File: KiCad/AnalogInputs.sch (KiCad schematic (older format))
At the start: 48 parts, among them J401 AI1, J402 AI2, J403 AI3, J404 AI4, J405 AI5, J406 AI6, J407 AI7, J408 AI8, U401 ADS1115IDGST, U402 ADS1115IDGST

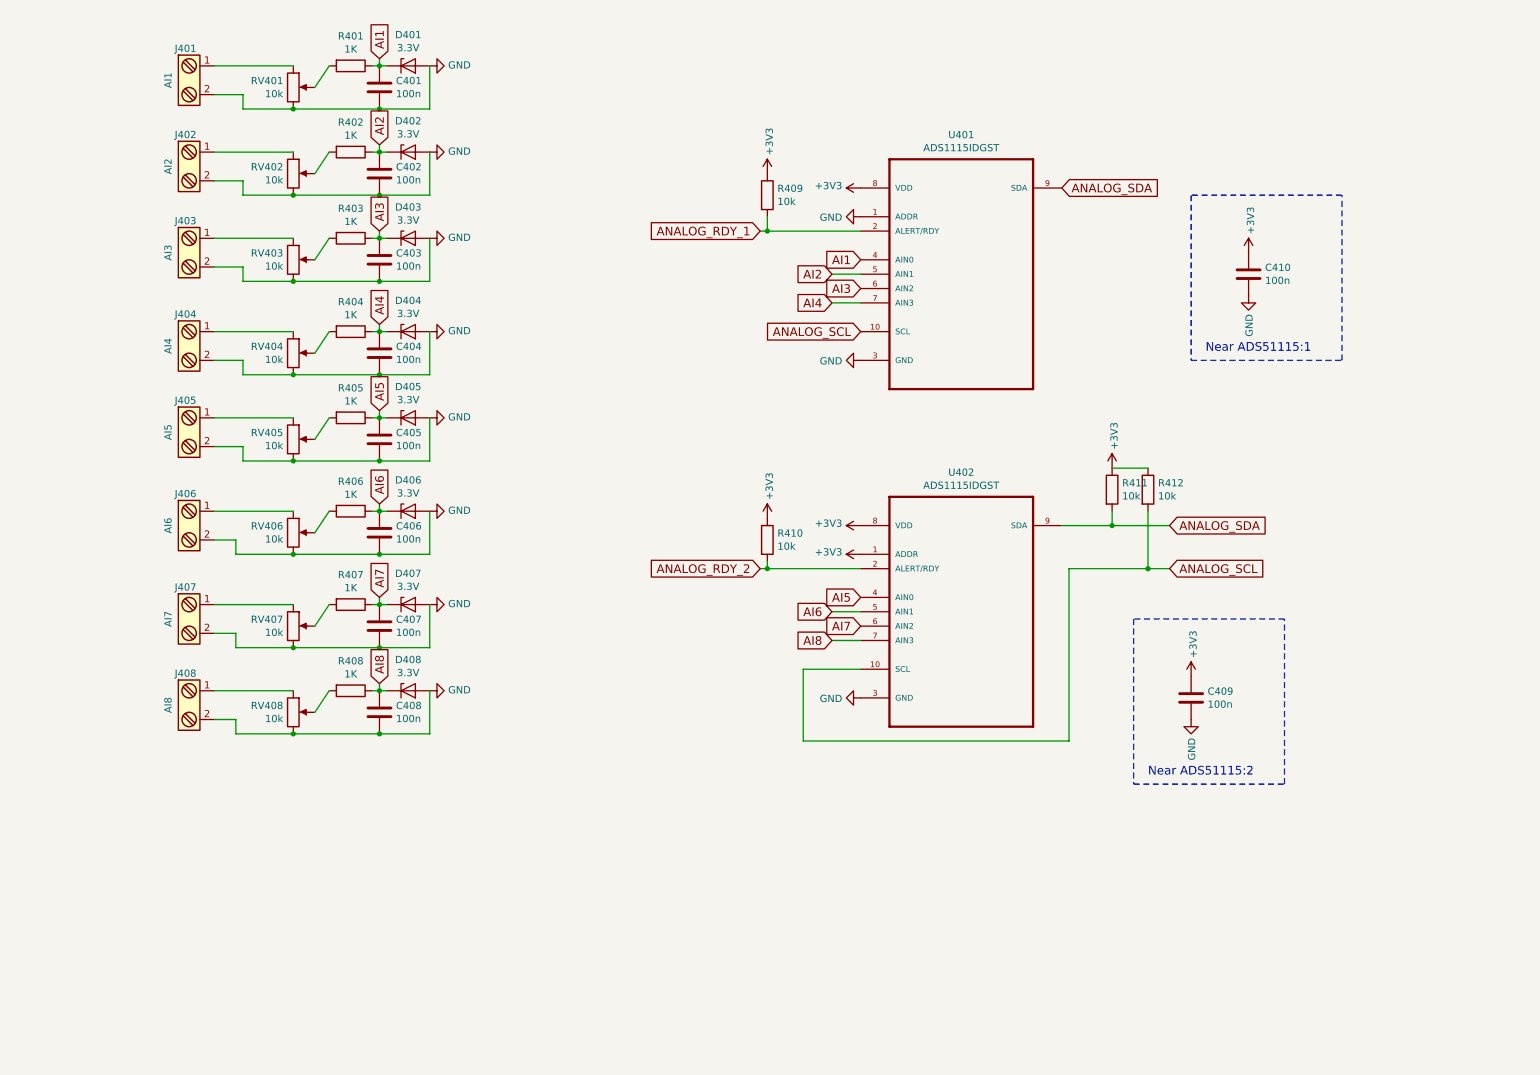
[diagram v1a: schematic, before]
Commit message: Save with sensor inputs using digital potentiometer
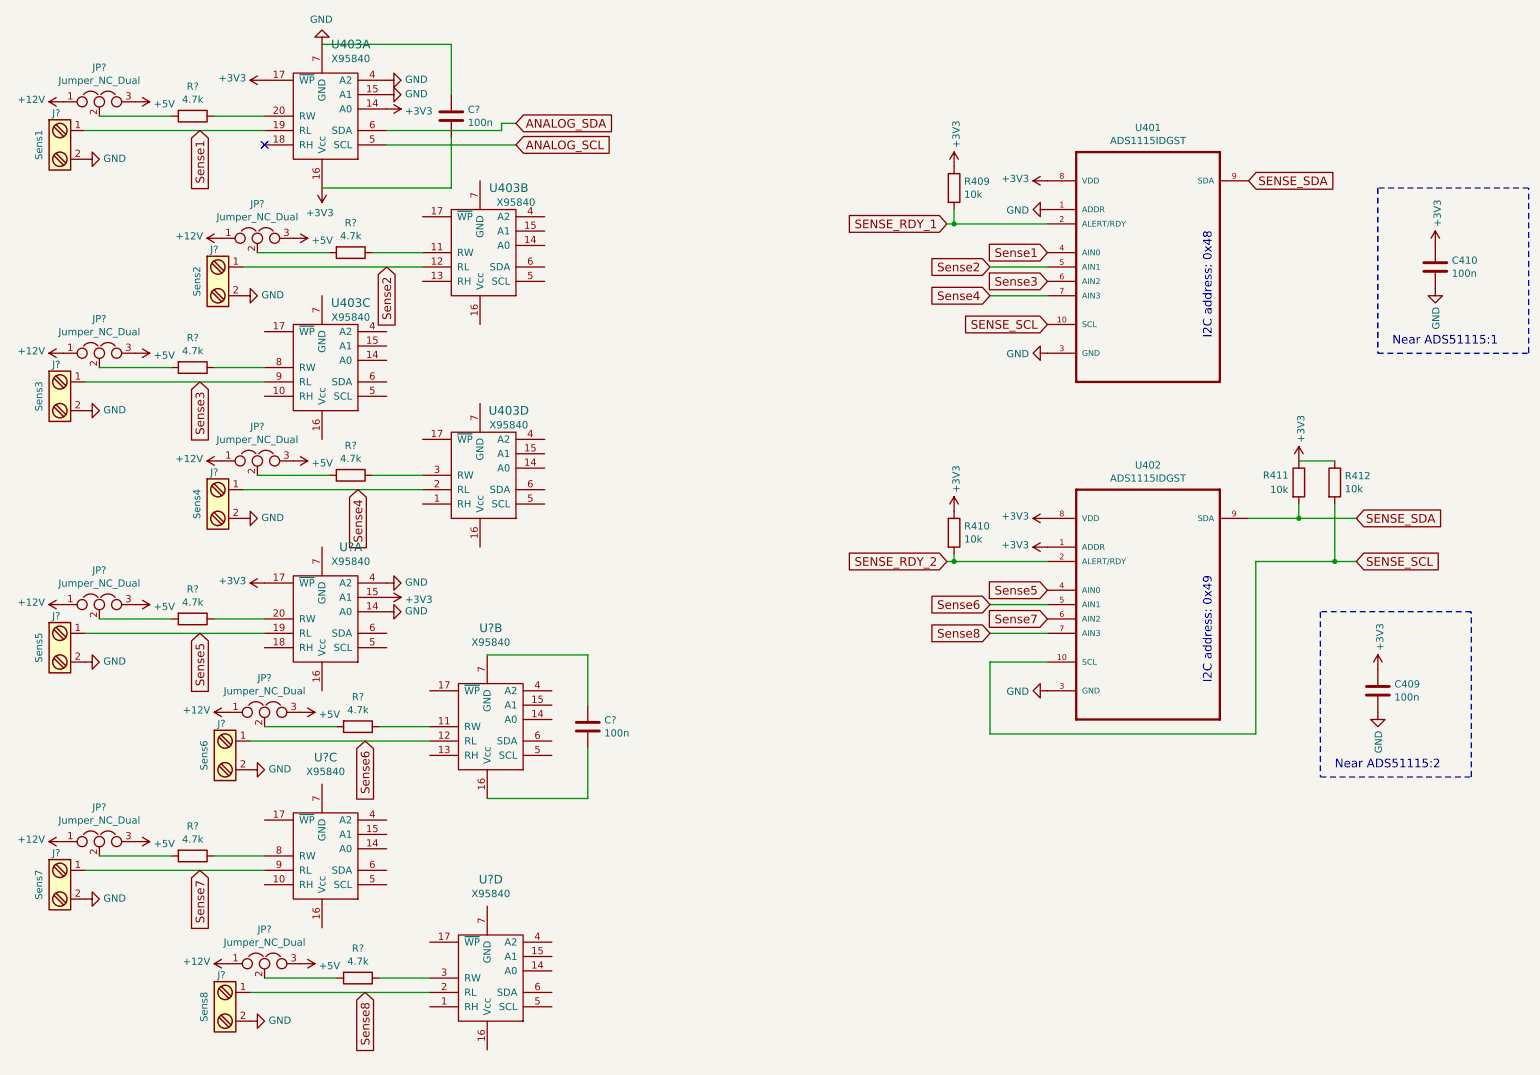
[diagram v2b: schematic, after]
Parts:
- removed C401, C402, C403, C404, C405, C406, C407, C408: 100n, Capacitors_SMD:C_0805, symbol C
- removed D401, D402, D403, D404, D405, D406, D407, D408: 3.3V, Diodes_SMD:D_SOT-23_ANK, symbol D_Zener
- removed J401: AI1, Connectors_Terminal_Blocks:TerminalBlock_Pheonix_MPT-2.54mm_2pol, symbol Screw_Terminal_1x02
- removed J402: AI2, Connectors_Terminal_Blocks:TerminalBlock_Pheonix_MPT-2.54mm_2pol, symbol Screw_Terminal_1x02
- removed J403: AI3, Connectors_Terminal_Blocks:TerminalBlock_Pheonix_MPT-2.54mm_2pol, symbol Screw_Terminal_1x02
- removed J404: AI4, Connectors_Terminal_Blocks:TerminalBlock_Pheonix_MPT-2.54mm_2pol, symbol Screw_Terminal_1x02
- removed J405: AI5, Connectors_Terminal_Blocks:TerminalBlock_Pheonix_MPT-2.54mm_2pol, symbol Screw_Terminal_1x02
- removed J406: AI6, Connectors_Terminal_Blocks:TerminalBlock_Pheonix_MPT-2.54mm_2pol, symbol Screw_Terminal_1x02
- removed J407: AI7, Connectors_Terminal_Blocks:TerminalBlock_Pheonix_MPT-2.54mm_2pol, symbol Screw_Terminal_1x02
- removed J408: AI8, Connectors_Terminal_Blocks:TerminalBlock_Pheonix_MPT-2.54mm_2pol, symbol Screw_Terminal_1x02
- removed R401, R402, R403, R404, R405, R406, R407, R408: 1K, Resistors_SMD:R_0805, symbol R
- removed RV401, RV402, RV403, RV404, RV405, RV406, RV407, RV408: 10k, Potentiometers:Potentiometer_WirePads_Small, symbol POT
- added C? (x2): 100n, Capacitors_SMD:C_0805, symbol C
- added J?: Sens1, Connectors_Terminal_Blocks:TerminalBlock_Pheonix_MPT-2.54mm_2pol, symbol Screw_Terminal_1x02
- added J?: Sens2, Connectors_Terminal_Blocks:TerminalBlock_Pheonix_MPT-2.54mm_2pol, symbol Screw_Terminal_1x02
- added J?: Sens3, Connectors_Terminal_Blocks:TerminalBlock_Pheonix_MPT-2.54mm_2pol, symbol Screw_Terminal_1x02
- added J?: Sens4, Connectors_Terminal_Blocks:TerminalBlock_Pheonix_MPT-2.54mm_2pol, symbol Screw_Terminal_1x02
- added J?: Sens5, Connectors_Terminal_Blocks:TerminalBlock_Pheonix_MPT-2.54mm_2pol, symbol Screw_Terminal_1x02
- added J?: Sens6, Connectors_Terminal_Blocks:TerminalBlock_Pheonix_MPT-2.54mm_2pol, symbol Screw_Terminal_1x02
- added J?: Sens7, Connectors_Terminal_Blocks:TerminalBlock_Pheonix_MPT-2.54mm_2pol, symbol Screw_Terminal_1x02
- added J?: Sens8, Connectors_Terminal_Blocks:TerminalBlock_Pheonix_MPT-2.54mm_2pol, symbol Screw_Terminal_1x02
- added JP? (x8): Jumper_NC_Dual, symbol Jumper_NC_Dual
- added R? (x8): 4.7k, symbol R
- added U403, U? (x4): X95840, symbol X95840
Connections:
- net +3V3: now also C?.2, U403.14 (A0), U403.16 (Vcc), U403.17 (~WP), U?.15 (A1), U?.17 (~WP)
- net ANALOG_SCL: now also U403.5 (SCL); no longer R412.2, U401.10 (SCL), U402.10 (SCL)
- net ANALOG_SDA: now also U403.6 (SDA); no longer R411.2, U401.9 (SDA), U402.9 (SDA)
- net GND: now also C?.1, J?.2, J?.2, J?.2, J?.2, J?.2, J?.2, J?.2, J?.2, U403.15 (A1), U403.4 (A2), U403.7 (GND), U?.14 (A0), U?.4 (A2)
- net AI1 renamed Sense1
- net Sense1: now also J?.1, U403.19 (RL)
- net AI2 renamed Sense2
- net Sense2: now also J?.1, U403.12 (RL)
- net AI3 renamed Sense3
- net Sense3: now also J?.1, U403.9 (RL)
- net AI4 renamed Sense4
- net Sense4: now also J?.1, U403.2 (RL)
- net AI5 renamed Sense5
- net Sense5: now also J?.1, U?.19 (RL)
- net AI6 renamed Sense6
- net Sense6: now also J?.1, U?.12 (RL)
- net AI7 renamed Sense7
- net Sense7: now also J?.1, U?.9 (RL)
- net AI8 renamed Sense8
- net Sense8: now also J?.1, U?.2 (RL)
- net ANALOG_RDY_1 renamed SENSE_RDY_1
- net ANALOG_RDY_2 renamed SENSE_RDY_2
- new net: R?.1, U403.20 (RW)
- new net: R?.1, U403.11 (RW)
- new net: R?.1, U403.8 (RW)
- new net: R?.1, U403.3 (RW)
- new net: JP?.2, R?.2 (x8)
- new net: R?.1, U?.20 (RW)
- new net: R?.1, U?.11 (RW)
- new net: C?.2, U?.16 (Vcc)
- new net: C?.1, U?.7 (GND)
- new net: R?.1, U?.8 (RW)
- new net: R?.1, U?.3 (RW)
- new net +12V: JP?.1, JP?.1, JP?.1, JP?.1, JP?.1, JP?.1, JP?.1, JP?.1
- new net +5V: JP?.3, JP?.3, JP?.3, JP?.3, JP?.3, JP?.3, JP?.3, JP?.3
- new net SENSE_SCL: R412.2, U401.10 (SCL), U402.10 (SCL)
- new net SENSE_SDA: R411.2, U401.9 (SDA), U402.9 (SDA)
- no-connect marks 0 -> 1
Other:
- note added: "I2C address: 0x48"
- note added: "I2C address: 0x49"
- moved on the sheet: C409, C410, R409, R410, R411, R412, U401, U402
